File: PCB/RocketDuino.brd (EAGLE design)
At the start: 73 x 41 mm, 41 parts, among them J1 FTDI, Y1 16MHZ

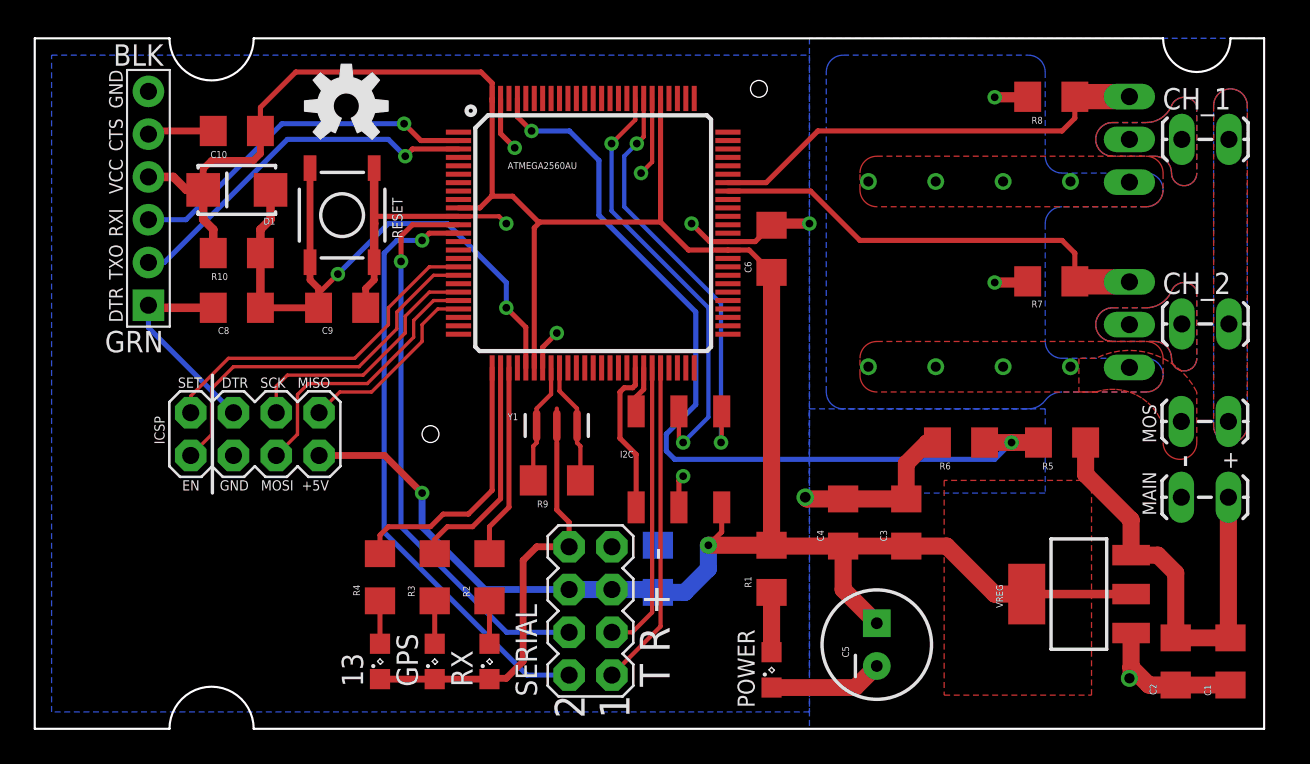
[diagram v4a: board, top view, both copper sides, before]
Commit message: Made C4 Explosive
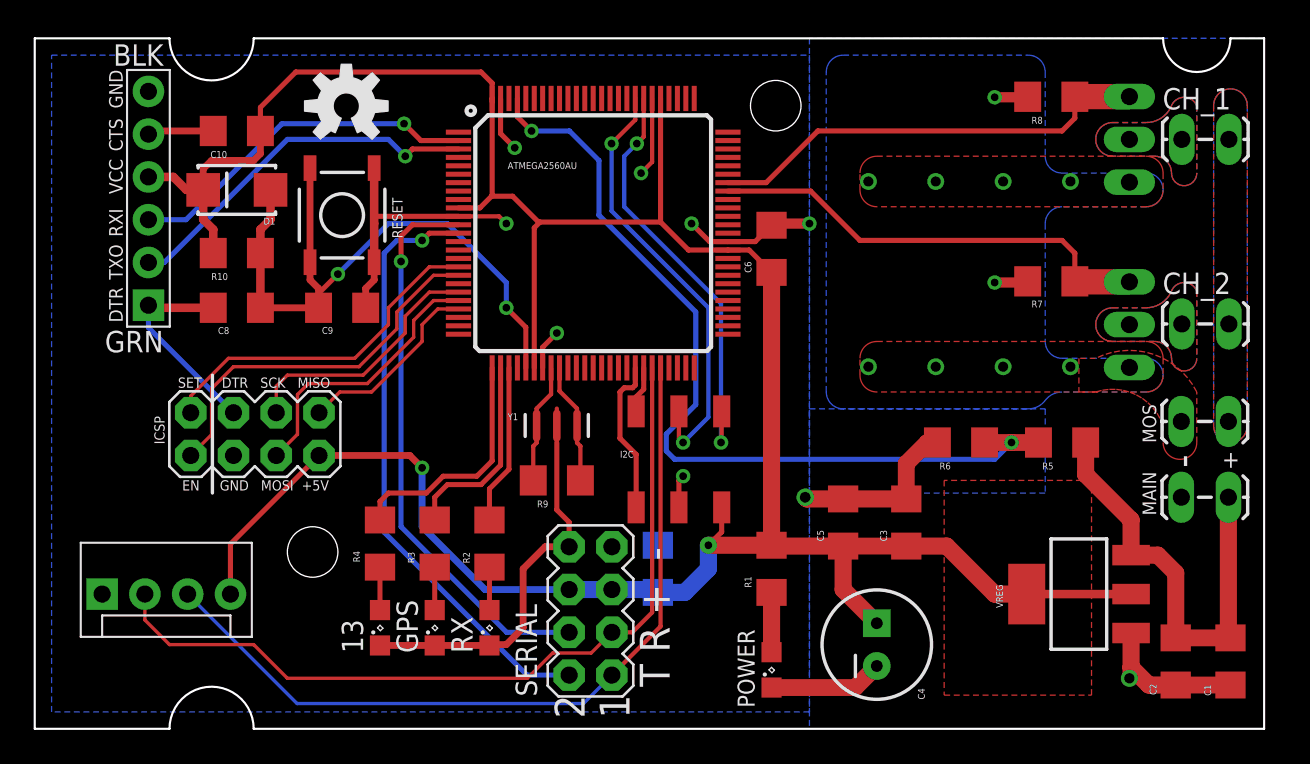
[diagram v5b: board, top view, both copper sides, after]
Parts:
- added J2: (no value), SparkFun-Connectors:MOLEX-1X4
- C4: value 0.1uF -> 470uF; device SparkFun-Capacitors:1206 -> SparkFun-Capacitors:CPOL-RADIAL-100UF-25V
- C5: value 470uF -> 0.1uF; device SparkFun-Capacitors:CPOL-RADIAL-100UF-25V -> SparkFun-Capacitors:1206
- moved C4 7.52 mm to (50.0, 5.00)
- moved C5 7.52 mm to (48.0, 12.2)
- moved 13 2.00 mm to (20.5, 6.00)
- moved GPS 2.00 mm to (23.8, 6.00)
- moved R2 2.00 mm to (27.0, 11.0)
- moved R3 2.00 mm to (23.8, 11.0)
- moved R4 2.00 mm to (20.5, 11.0)
- moved RX 2.00 mm to (27.0, 6.00)
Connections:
- net 5V: now also J2.4
- net GND: now also J2.1
- net RX1: now also J2.2
- net TX1: now also J2.3
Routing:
- net RX1: track 17.4 -> 49.2 mm
- net TX1: track 19.4 -> 48.0 mm
- net 5V: track 155.1 -> 166.4 mm
- net GND: track 96.0 -> 93.7 mm
- net LED_RX: track 11.5 -> 9.51 mm
- net LED_13: track 16.1 -> 14.3 mm
- net LED_GPS: track 13.5 -> 11.8 mm

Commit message: Seperated Serial 1 & 2
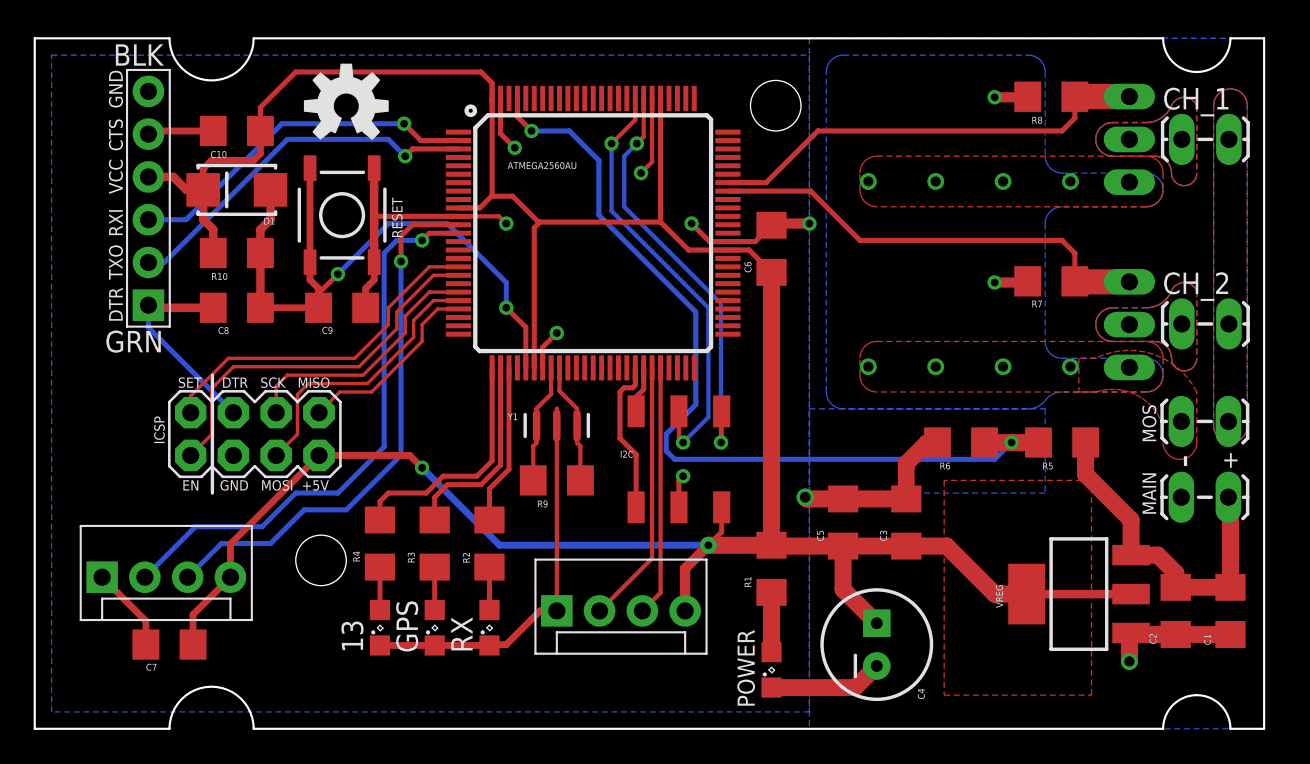
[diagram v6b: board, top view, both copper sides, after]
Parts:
- removed J2: (no value), SparkFun-Connectors:MOLEX-1X4
- removed SERIAL: (no value), SparkFun-Connectors:2X4
- added SERIAL1, SERIAL2: (no value), SparkFun-Connectors:MOLEX-1X4
- moved C7 29.3 mm to (8.00, 5.00), flipped to the top, turned to 180 degrees
- moved C1 3.00 mm to (71.0, 7.00)
- moved C2 3.00 mm to (67.8, 7.00)
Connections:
- net 5V: now also SERIAL1.4, SERIAL2.4; no longer J2.4, SERIAL.5, SERIAL.6
- net GND: now also SERIAL1.1, SERIAL2.1; no longer J2.1, SERIAL.7, SERIAL.8
- net RX1: now also SERIAL1.2; no longer J2.2, SERIAL.3
- net RX2: now also SERIAL2.3; no longer SERIAL.4
- net TX1: now also SERIAL1.3; no longer J2.3, SERIAL.1
- net TX2: now also SERIAL2.2; no longer SERIAL.2
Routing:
- net RX1: track 49.2 -> 15.7 mm
- net TX1: track 48.0 -> 14.9 mm
- net VIN: track 26.8 -> 20.8 mm
- net 5V: track 166.4 -> 169.4 mm
- net GND: track 93.7 -> 96.5 mm
- net TX2: track 36.0 -> 33.8 mm
- net RX2: track 33.5 -> 32.4 mm
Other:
- outline, holes or cut-outs redrawn
- board text removed: "2 1"
- board text removed: "T R + -"

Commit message: Revert "Revert "Add Labels (2)""
This reverts commit 35d22b4ccda85a27ff9208a5b721f9a8abebe91e.
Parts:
- renumbered 13 to INFO
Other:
- board text added: "GND RX TX 5V"
- board text added: "GND TX RX 5V"
- board text added: "Serial 1"
- board text added: "Serial 2"
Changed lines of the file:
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@@
 <wire x1="69" y1="2" x2="71" y2="0" width="0.127" layer="20" curve="-90"/>
 <wire x1="67" y1="0" x2="69" y2="2" width="0.127" layer="20" curve="-90"/>
+<text x="30" y="3" size="0.8128" layer="21">GND  RX   TX    5V</text>
+<text x="3" y="12.5" size="0.8128" layer="21">GND  TX   RX    5V</text>
+<text x="28.5" y="9" size="1.016" layer="21" rot="R270">Serial 1</text>
+<text x="1.5" y="11.25" size="1.016" layer="21" rot="R270">Serial 2</text>
 </plain>
 <attributes>
@@
 <element name="D1" library="SparkFun-DiscreteSemi" package="SMA-DIODE_ALT" value="" x="12" y="32" rot="R180"/>
 <element name="LOGO1" library="SparkFun-Aesthetics" package="OSHW-LOGO-M" value="OSHW-LOGOM" x="18.5" y="36.98"/>
-<element name="13" library="led" package="SML0805" value="" x="20.5" y="6" rot="R90"/>
+<element name="INFO" library="led" package="SML0805" value="" x="20.5" y="6" rot="R90"/>
 <element name="MOS" library="SparkFun-Connectors" package="1X02_LOCK_LONGPADS" value="" x="70.75" y="18.25" locked="yes" smashed="yes" rot="R180">
 <attribute name="NAME" x="65.778" y="19.27" size="0.8128" layer="25" font="vector" rot="R270"/>
@@
 <contactref element="J1" pad="P$6"/>
 <contactref element="J1" pad="P$5"/>
-<contactref element="13" pad="C"/>
+<contactref element="INFO" pad="C"/>
 <contactref element="ATMEGA2560AU" pad="32"/>
 <contactref element="ATMEGA2560AU" pad="11"/>
@@
 </signal>
 <signal name="N$3">
-<contactref element="13" pad="A"/>
+<contactref element="INFO" pad="A"/>
 <contactref element="R4" pad="1"/>
 <wire x1="20.5" y1="9.6" x2="20.5" y2="7.05" width="0.3" layer="1"/>

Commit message: New DRU settings
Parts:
- moved C2 0.25 mm to (68.0, 7.00)
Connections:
- net RX2: now also SERIAL2.2; no longer SERIAL2.3
- net TX2: now also SERIAL2.3; no longer SERIAL2.2
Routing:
- net TX2: track 33.8 -> 31.9 mm
- net RX2: track 32.4 -> 34.0 mm
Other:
- board text removed: "GND TX RX 5V"
